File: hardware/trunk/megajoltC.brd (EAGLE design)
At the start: 79.9 x 63 mm, 117 parts, among them IC1 IC_FT230X-SSOP-16, IC2 MCP1826, IC3 MCP1826, J3 JUMPER_CLOSEDTHICK, U1 MCP1700, U11 TLV274, U12 PESDXS4UD, U18 MCP2551SO8, U4 ZXMS6004FF, U8 FAN8303, X1 MINI_USB_SHIELD

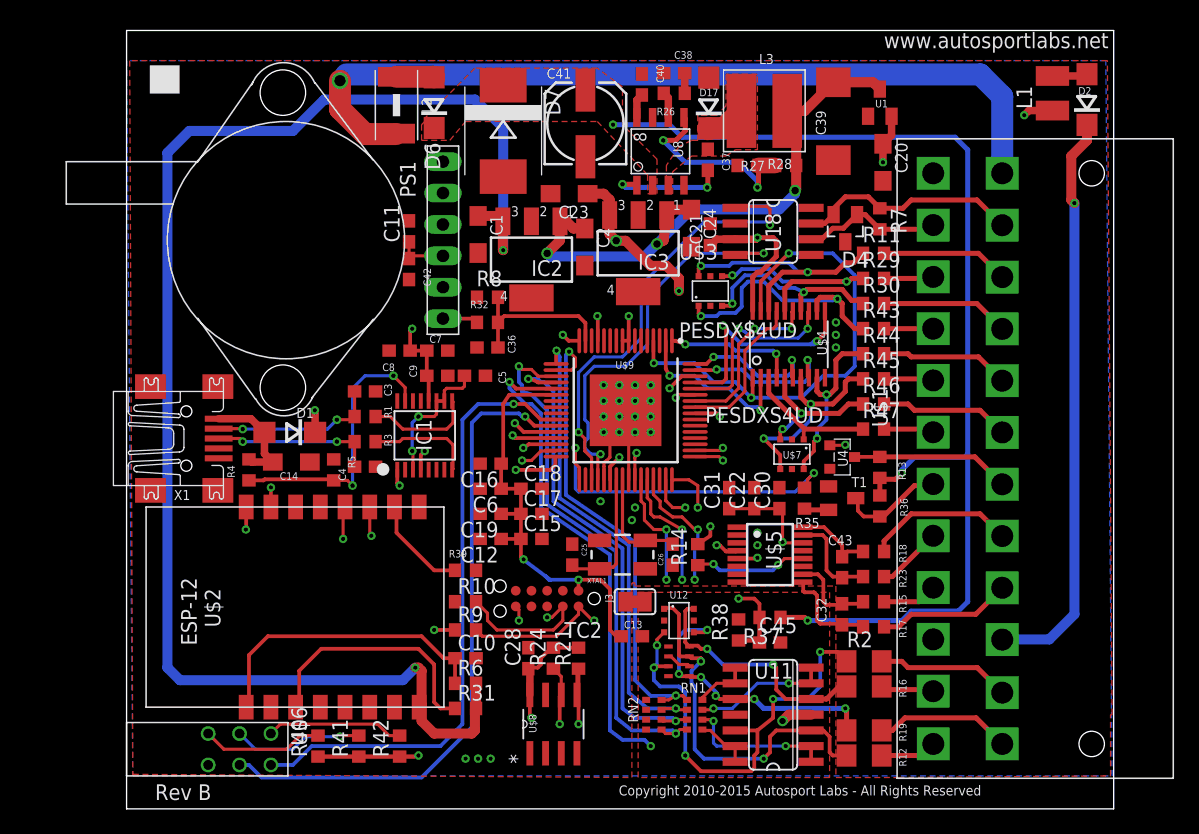
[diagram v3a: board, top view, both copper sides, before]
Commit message: Fix minor grounding issue
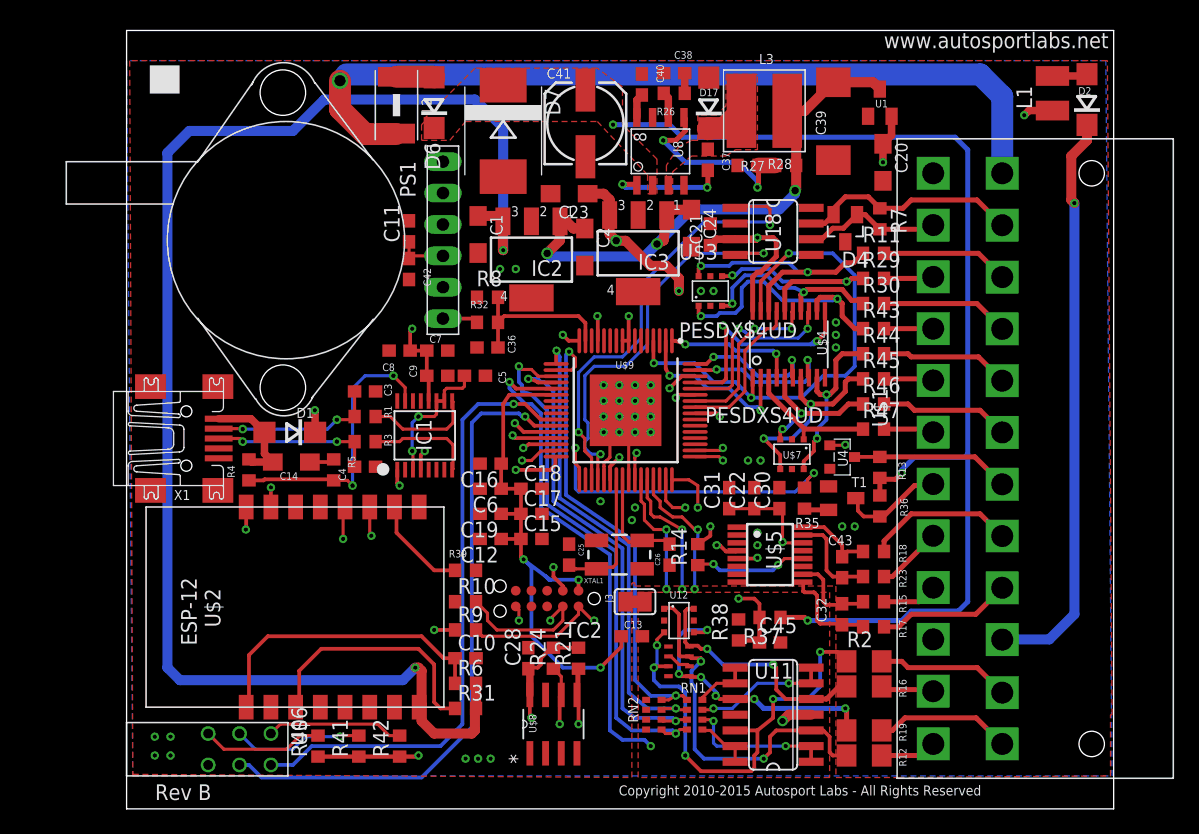
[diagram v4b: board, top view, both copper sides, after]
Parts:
- moved C25 0.25 mm to (35.8, 20.6)
- moved C26 0.25 mm to (43.9, 20.6)
- moved XTAL1 0.25 mm to (39.9, 20.6)
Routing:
- net +3V3: track 79.4 -> 88.5 mm, vias 12 -> 13
- net GND: track 12.7 -> 16.9 mm, vias 24 -> 37
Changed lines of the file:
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@@
 <element name="C18" library="resistor" package="C0603" value="100nF" x="32.766" y="25.908"/>
 <element name="C19" library="resistor" package="C0603" value="100nF" x="29.464" y="23.876" rot="R180"/>
-<element name="XTAL1" library="SparkFun2" package="CRYSTAL-SMD-5X3" value="8MHz" x="40.132" y="20.574" smashed="yes" rot="R180">
-<attribute name="NAME" x="38.862" y="18.669" size="0.4064" layer="25" rot="R180"/>
-<attribute name="VALUE" x="42.672" y="23.114" size="0.4064" layer="27" rot="R180"/>
-</element>
-<element name="C25" library="SparkFun" package="0603" value="33pF" x="36.068" y="20.574" rot="R270"/>
-<element name="C26" library="SparkFun" package="0603" value="33pF" x="44.196" y="20.574" rot="R90"/>
+<element name="XTAL1" library="SparkFun2" package="CRYSTAL-SMD-5X3" value="8MHz" x="39.878" y="20.574" smashed="yes" rot="R180">
+<attribute name="NAME" x="38.608" y="18.669" size="0.4064" layer="25" rot="R180"/>
+<attribute name="VALUE" x="42.418" y="23.114" size="0.4064" layer="27" rot="R180"/>
+</element>
+<element name="C25" library="SparkFun" package="0603" value="33pF" x="35.814" y="20.574" rot="R270"/>
+<element name="C26" library="SparkFun" package="0603" value="33pF" x="43.942" y="20.574" rot="R90"/>
 <element name="J3" library="jumpers" package="JUMPER_CLOSED_THICK" value="JUMPER_CLOSEDTHICK" x="41.148" y="16.764" smashed="yes" rot="R180">
 <attribute name="NAME" x="38.735" y="17.399" size="0.6096" layer="25" ratio="10" rot="R270"/>
@@
 <via x="41.148" y="34.29" extent="1-16" drill="0.3302"/>
 <via x="41.148" y="33.02" extent="1-16" drill="0.3302"/>
-<wire x1="14.835" y1="28.067" x2="16.764" y2="28.282" width="0" layer="19" extent="1-1"/>
-<wire x1="40.386" y1="16.764" x2="35.306" y2="17.653" width="0" layer="19" extent="1-1"/>
-<wire x1="44.196" y1="19.724" x2="40.386" y2="16.764" width="0" layer="19" extent="1-1"/>
+<wire x1="35.306" y1="17.653" x2="35.306" y2="18.034" width="0.3048" layer="1"/>
+<wire x1="35.306" y1="18.034" x2="34.544" y2="18.796" width="0.3048" layer="1"/>
+<wire x1="34.544" y1="18.796" x2="34.544" y2="19.558" width="0.3048" layer="1"/>
+<via x="34.544" y="19.558" extent="1-16" drill="0.3302"/>
+<wire x1="14.835" y1="28.067" x2="16.549" y2="28.067" width="0.3048" layer="1"/>
+<wire x1="16.549" y1="28.067" x2="16.764" y2="28.282" width="0.3048" layer="1"/>
+<via x="57.912" y="22.86" extent="1-16" drill="0.3302"/>
+<via x="58.928" y="22.86" extent="1-16" drill="0.3302"/>
+<via x="50.292" y="28.194" extent="1-16" drill="0.3302"/>
+<via x="51.308" y="28.194" extent="1-16" drill="0.3302"/>
+<via x="46.482" y="41.91" extent="1-16" drill="0.3302"/>
+<via x="47.498" y="41.91" extent="1-16" drill="0.3302"/>
+<via x="31.496" y="43.688" extent="1-16" drill="0.3302"/>
+<via x="30.226" y="43.688" extent="1-16" drill="0.3302"/>
+<via x="2.286" y="5.842" extent="1-16" drill="0.3302"/>
+<via x="3.556" y="5.842" extent="1-16" drill="0.3302"/>
+<via x="3.556" y="4.318" extent="1-16" drill="0.3302"/>
+<via x="2.286" y="4.318" extent="1-16" drill="0.3302"/>
 </signal>
 <signal name="+5V">
@@
 <wire x1="32.639" y1="7.493" x2="32.766" y2="7.366" width="0.3048" layer="1"/>
 <via x="32.766" y="7.366" extent="1-16" drill="0.3302"/>
-<wire x1="40.044" y1="13.97" x2="39.624" y2="13.97" width="0.3048" layer="1"/>
-<wire x1="39.624" y1="13.97" x2="39.116" y2="14.478" width="0.3048" layer="1"/>
-<wire x1="39.116" y1="14.478" x2="39.116" y2="17.78" width="0.3048" layer="1"/>
-<wire x1="39.116" y1="17.78" x2="38.354" y2="18.542" width="0.3048" layer="1"/>
 <wire x1="36.576" y1="17.653" x2="36.576" y2="18.542" width="0.3048" layer="1"/>
 <via x="36.576" y="18.542" extent="1-16" drill="0.3302"/>
@@
 <wire x1="34.29" y1="18.542" x2="33.8836" y2="18.8468" width="0.3048" layer="16"/>
 <wire x1="33.8836" y1="18.8468" x2="32.258" y2="20.066" width="0.3048" layer="16"/>
-<wire x1="38.354" y1="18.542" x2="36.576" y2="18.542" width="0.3048" layer="1"/>
 <wire x1="24.447" y1="33.005" x2="24.447" y2="34.989" width="0.3048" layer="1"/>
 <wire x1="24.447" y1="34.989" x2="24.384" y2="35.052" width="0.3048" layer="1"/>
@@
 <wire x1="39.136" y1="27.706" x2="39.878" y2="28.448" width="0.3048" layer="1"/>
 <via x="39.878" y="28.448" extent="1-16" drill="0.3302"/>
+<wire x1="32.766" y1="13.97" x2="32.766" y2="19.558" width="0.3048" layer="16"/>
+<wire x1="32.766" y1="19.558" x2="32.131" y2="20.193" width="0.3048" layer="16"/>
+<wire x1="40.044" y1="13.97" x2="40.044" y2="13.12" width="0.3048" layer="1"/>
+<wire x1="40.044" y1="13.12" x2="38.354" y2="11.43" width="0.3048" layer="1"/>
+<via x="38.354" y="11.43" extent="1-16" drill="0.3302"/>
+<wire x1="38.354" y1="11.43" x2="35.306" y2="11.43" width="0.3048" layer="16"/>
+<wire x1="35.306" y1="11.43" x2="32.766" y2="13.97" width="0.3048" layer="16"/>
 </signal>
 <signal name="FTDI_DM">
@@
 <wire x1="40.136" y1="22.094" x2="40.64" y2="21.59" width="0.254" layer="1"/>
 <wire x1="40.64" y1="21.59" x2="41.848" y2="21.59" width="0.254" layer="1"/>
-<wire x1="41.848" y1="21.59" x2="41.982" y2="21.724" width="0.254" layer="1"/>
-<wire x1="41.982" y1="21.724" x2="43.896" y2="21.724" width="0.254" layer="1"/>
-<wire x1="43.896" y1="21.724" x2="44.196" y2="21.424" width="0.254" layer="1"/>
+<wire x1="41.848" y1="21.59" x2="41.728" y2="21.724" width="0.254" layer="1"/>
+<wire x1="41.728" y1="21.724" x2="43.896" y2="21.724" width="0.254" layer="1"/>
+<wire x1="43.896" y1="21.724" x2="43.942" y2="21.424" width="0.254" layer="1"/>
 <contactref element="U$9" pad="40"/>
 <wire x1="40.136" y1="22.094" x2="40.136" y2="26.633" width="0.254" layer="1"/>
@@
 <wire x1="39.636" y1="19.824" x2="39.37" y2="19.558" width="0.254" layer="1"/>
 <wire x1="39.37" y1="19.558" x2="38.416" y2="19.558" width="0.254" layer="1"/>
-<wire x1="38.416" y1="19.558" x2="38.282" y2="19.424" width="0.254" layer="1"/>
-<wire x1="38.282" y1="19.424" x2="36.368" y2="19.424" width="0.254" layer="1"/>
-<wire x1="36.368" y1="19.424" x2="36.068" y2="19.724" width="0.254" layer="1"/>
+<wire x1="38.416" y1="19.558" x2="38.028" y2="19.424" width="0.254" layer="1"/>
+<wire x1="38.028" y1="19.424" x2="36.368" y2="19.424" width="0.254" layer="1"/>
+<wire x1="36.368" y1="19.424" x2="35.814" y2="19.724" width="0.254" layer="1"/>
 <contactref element="U$9" pad="39"/>
 <wire x1="39.636" y1="26.633" x2="39.636" y2="19.824" width="0.254" layer="1"/>
@@
 <wire x1="42.672" y1="22.606" x2="43.688" y2="22.606" width="0.254" layer="1"/>
 <via x="43.688" y="22.606" extent="1-16" drill="0.3302"/>
-<wire x1="43.688" y1="22.606" x2="43.688" y2="18.542" width="0.254" layer="16"/>
-<via x="43.688" y="18.542" extent="1-16" drill="0.3302"/>
-<wire x1="43.688" y1="18.542" x2="37.846" y2="18.542" width="0.254" layer="15"/>
-<wire x1="37.846" y1="18.542" x2="37.084" y2="17.78" width="0.254" layer="15"/>
-<wire x1="37.084" y1="17.78" x2="34.29" y2="17.78" width="0.254" layer="15"/>
+<wire x1="43.688" y1="22.606" x2="43.688" y2="17.78" width="0.254" layer="16"/>
+<via x="43.688" y="17.78" extent="1-16" drill="0.3302"/>
+<wire x1="43.688" y1="17.78" x2="34.29" y2="17.78" width="0.254" layer="15"/>
 <wire x1="34.29" y1="17.78" x2="31.75" y2="15.24" width="0.254" layer="15"/>
 <via x="31.75" y="15.24" extent="1-16" drill="0.3302"/>
@@
 <wire x1="46.228" y1="22.606" x2="46.228" y2="21.844" width="0.254" layer="16"/>
 <wire x1="46.228" y1="21.844" x2="45.974" y2="21.59" width="0.254" layer="16"/>
-<wire x1="45.974" y1="21.59" x2="45.974" y2="18.542" width="0.254" layer="16"/>
-<via x="45.974" y="18.542" extent="1-16" drill="0.3302"/>
-<wire x1="45.974" y1="18.542" x2="45.974" y2="16.764" width="0.254" layer="15"/>
+<wire x1="45.974" y1="21.59" x2="45.974" y2="17.78" width="0.254" layer="16"/>
+<via x="45.974" y="17.78" extent="1-16" drill="0.3302"/>
+<wire x1="45.974" y1="17.78" x2="45.974" y2="16.764" width="0.254" layer="15"/>
 <wire x1="45.974" y1="16.764" x2="44.958" y2="15.748" width="0.254" layer="15"/>
 <wire x1="44.958" y1="15.748" x2="40.132" y2="15.748" width="0.254" layer="15"/>
 <wire x1="40.132" y1="15.748" x2="38.608" y2="14.224" width="0.254" layer="15"/>
 <wire x1="38.608" y1="14.224" x2="35.306" y2="14.224" width="0.254" layer="15"/>
-<wire x1="35.306" y1="14.224" x2="34.036" y2="15.494" width="0.254" layer="15"/>
-<via x="34.036" y="15.494" extent="1-16" drill="0.3302"/>
-<wire x1="34.036" y1="15.494" x2="34.417" y2="15.494" width="0.254" layer="1"/>
+<wire x1="35.306" y1="14.224" x2="34.29" y2="15.24" width="0.254" layer="15"/>
+<via x="34.29" y="15.24" extent="1-16" drill="0.3302"/>
+<wire x1="34.29" y1="15.24" x2="34.417" y2="15.494" width="0.254" layer="1"/>
 <wire x1="34.417" y1="15.494" x2="35.306" y2="16.383" width="0.254" layer="1"/>
 </signal>
@@
 <wire x1="43.18" y1="23.622" x2="44.958" y2="22.606" width="0.254" layer="1"/>
 <via x="44.958" y="22.606" extent="1-16" drill="0.3302"/>
-<wire x1="44.958" y1="22.606" x2="44.958" y2="18.542" width="0.254" layer="16"/>
-<via x="44.958" y="18.542" extent="1-16" drill="0.3302"/>
-<wire x1="44.958" y1="18.542" x2="44.958" y2="16.764" width="0.254" layer="15"/>
+<wire x1="44.958" y1="22.606" x2="44.958" y2="17.78" width="0.254" layer="16"/>
+<via x="44.958" y="17.78" extent="1-16" drill="0.3302"/>
+<wire x1="44.958" y1="17.78" x2="44.958" y2="16.764" width="0.254" layer="15"/>
 <wire x1="44.958" y1="16.764" x2="44.704" y2="16.51" width="0.254" layer="15"/>
 <wire x1="44.704" y1="16.51" x2="39.116" y2="16.51" width="0.254" layer="15"/>

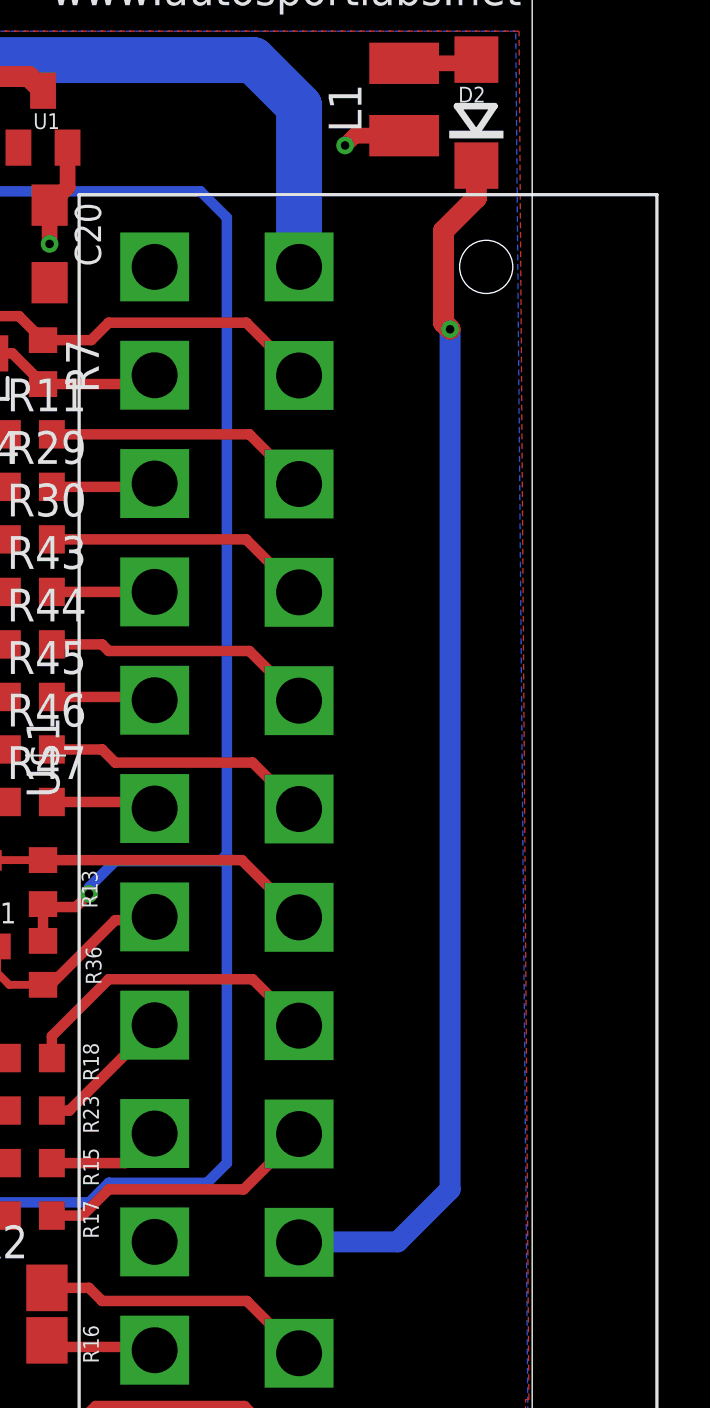
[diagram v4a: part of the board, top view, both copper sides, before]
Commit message: Fix DRC Dimension issue
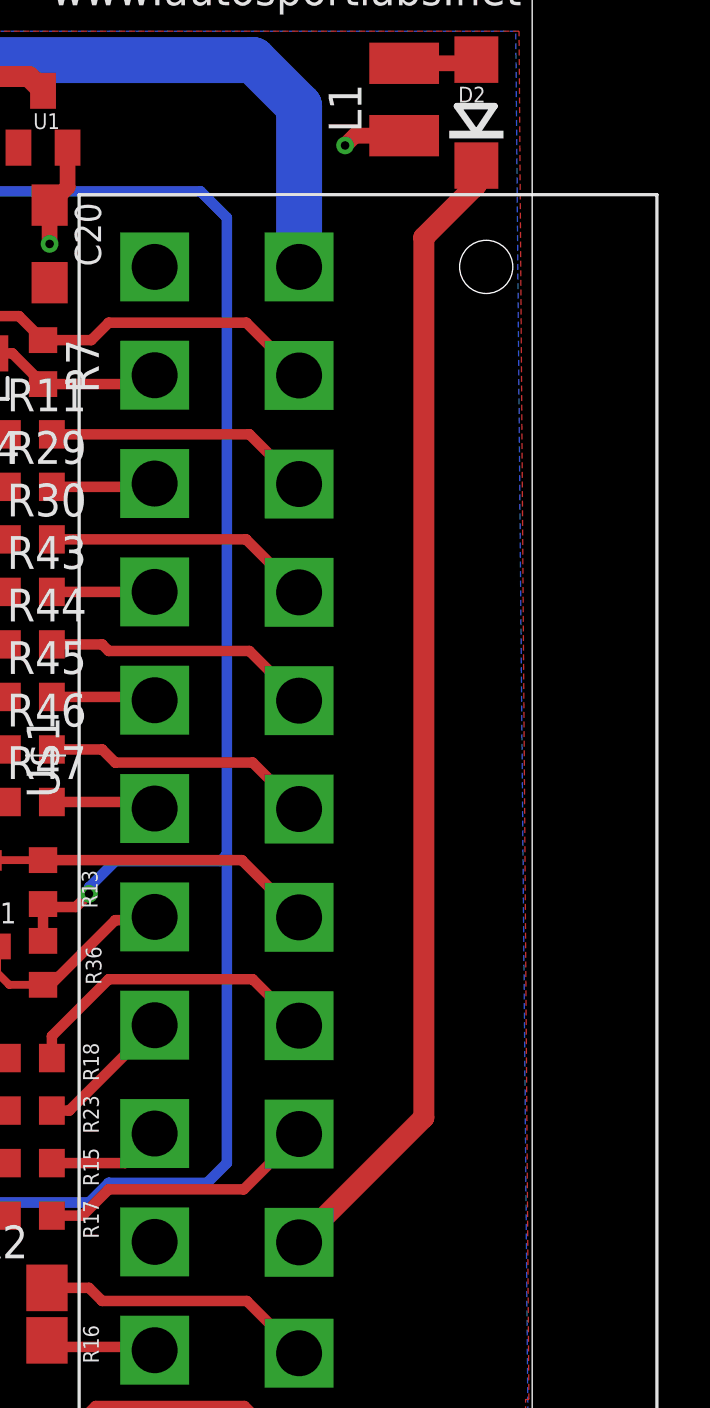
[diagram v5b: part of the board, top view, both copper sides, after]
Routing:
- net VREF: track 46.9 -> 44.5 mm, vias 1 -> 0
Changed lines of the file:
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@@
 <contactref element="U$1" pad="P15"/>
 <contactref element="D2" pad="C"/>
-<wire x1="77.724" y1="55.354" x2="77.724" y2="54.102" width="0.8128" layer="1"/>
-<wire x1="77.724" y1="54.102" x2="76.454" y2="52.832" width="0.8128" layer="1"/>
-<wire x1="76.454" y1="52.832" x2="76.454" y2="49.276" width="0.8128" layer="1"/>
-<wire x1="76.454" y1="49.276" x2="76.708" y2="49.022" width="0.8128" layer="1"/>
-<via x="76.708" y="49.022" extent="1-16" drill="0.3302"/>
-<wire x1="76.708" y1="49.022" x2="76.708" y2="15.748" width="0.8128" layer="16"/>
-<wire x1="76.708" y1="15.748" x2="74.676" y2="13.716" width="0.8128" layer="16"/>
-<wire x1="74.676" y1="13.716" x2="70.884" y2="13.716" width="0.8128" layer="16"/>
 <wire x1="70.884" y1="13.716" x2="70.866" y2="13.698" width="0.8128" layer="16"/>
+<wire x1="77.724" y1="55.354" x2="77.724" y2="54.61" width="0.8128" layer="1"/>
+<wire x1="77.724" y1="54.61" x2="75.692" y2="52.578" width="0.8128" layer="1"/>
+<wire x1="75.692" y1="52.578" x2="75.692" y2="18.524" width="0.8128" layer="1"/>
+<wire x1="75.692" y1="18.524" x2="70.866" y2="13.698" width="0.8128" layer="1"/>
 </signal>
 <signal name="+3V3">
@@
 <wire x1="43.688" y1="22.606" x2="43.688" y2="17.78" width="0.254" layer="16"/>
 <via x="43.688" y="17.78" extent="1-16" drill="0.3302"/>
-<wire x1="43.688" y1="17.78" x2="34.29" y2="17.78" width="0.254" layer="15"/>
+<wire x1="43.688" y1="17.78" x2="39.116" y2="17.78" width="0.254" layer="15"/>
+<wire x1="39.116" y1="17.78" x2="38.608" y2="18.288" width="0.254" layer="15"/>
+<wire x1="38.608" y1="18.288" x2="37.338" y2="18.288" width="0.254" layer="15"/>
+<wire x1="37.338" y1="18.288" x2="36.83" y2="17.78" width="0.254" layer="15"/>
+<wire x1="36.83" y1="17.78" x2="34.29" y2="17.78" width="0.254" layer="15"/>
 <wire x1="34.29" y1="17.78" x2="31.75" y2="15.24" width="0.254" layer="15"/>
 <via x="31.75" y="15.24" extent="1-16" drill="0.3302"/>
